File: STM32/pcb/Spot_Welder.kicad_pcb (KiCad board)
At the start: 2 copper layers, 100 x 60 mm, 63 parts, among them J1 SSD1306, J5 Battery, J6 Foot_Switch, SW1 RE, U1 HY4903B6, U10 HY4903B6, U11 HY4903B6, U2 STM32F030F4Px, U3 AMS1117-3.3, U4 ZXGD3009E6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

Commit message: pcb update
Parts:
- added C1: 10u, Capacitor_SMD:C_0805_2012Metric, F.Cu at (115.0, 164.0)
- added D18: TVS_SMDJ13A, Diode_SMD:D_SMC, B.Cu at (124.0, 130.0)
- added D19: TVS_SMDJ13A, Diode_SMD:D_SMC, B.Cu at (100.0, 130.0)
- added D20: TVS_SMDJ13A, Diode_SMD:D_SMC, B.Cu at (112.0, 130.0)
- added D21: TVS_SMDJ13A, Diode_SMD:D_SMC, B.Cu at (88.0, 130.0)
- added H1: MountingHole_Pad, MountingHole:MountingHole_6mm_Pad_Via, F.Cu at (125.0, 110.0)
- added H10: MountingHole_Pad, MountingHole:MountingHole_6mm_Pad_Via, F.Cu at (105.0, 150.0)
- added H11: MountingHole_Pad, MountingHole:MountingHole_6mm_Pad_Via, F.Cu at (145.0, 150.0)
- added H12: MountingHole_Pad, MountingHole:MountingHole_6mm_Pad_Via, F.Cu at (165.0, 150.0)
- added H2: MountingHole_Pad, MountingHole:MountingHole_6mm_Pad_Via, F.Cu at (105.0, 110.0)
- added H3: MountingHole, MountingHole:MountingHole_2.5mm, F.Cu at (177.0, 177.0)
- added H4: MountingHole, MountingHole:MountingHole_2.5mm, F.Cu at (177.0, 93.0)
- added H5: MountingHole, MountingHole:MountingHole_2.5mm, F.Cu at (83.0, 93.0)
- added H6: MountingHole, MountingHole:MountingHole_2.5mm, F.Cu at (83.0, 177.0)
- added H7: MountingHole_Pad, MountingHole:MountingHole_6mm_Pad_Via, F.Cu at (165.0, 110.0)
- added H8: MountingHole_Pad, MountingHole:MountingHole_6mm_Pad_Via, F.Cu at (145.0, 110.0)
- added H9: MountingHole_Pad, MountingHole:MountingHole_6mm_Pad_Via, F.Cu at (125.0, 150.0)
- added R21: 4.7k, Resistor_SMD:R_0603_1608Metric, F.Cu at (146.0, 168.0)
- added R22: 4.7k, Resistor_SMD:R_0603_1608Metric, F.Cu at (146.0, 170.0)
- C6: value 1u -> 10u; footprint Capacitor_SMD:C_0603_1608Metric -> Capacitor_SMD:C_0805_2012Metric
- C7: value 1u -> 22u; footprint Capacitor_SMD:C_0603_1608Metric -> Capacitor_SMD:C_1206_3216Metric
- D10, D11, D12, D13, D14, D15, D16, D17, D5, D7, D8, D9: moved to B.Cu
- R13, R14, R15, R16, R17, R18, R19, R20: value 100 -> 22; moved to B.Cu
- moved U4 117.7 mm to (173.0, 169.0), turned to 90 degrees
- moved U11 115.5 mm to (172.0, 130.0), turned to 90 degrees
- moved SW1 107.7 mm to (158.0, 177.0), turned to 90 degrees
- moved R17 106.4 mm to (160.0, 138.0)
- moved R20 102.7 mm to (172.0, 138.0)
- moved R14 99.2 mm to (148.0, 138.0)
- moved C10 98.4 mm to (174.0, 163.0), turned to 90 degrees
- moved R5 96.9 mm to (178.0, 163.0), turned to -90 degrees
- moved R8 96.6 mm to (170.0, 175.0)
- moved D4 94.0 mm to (171.0, 163.0), turned to 180 degrees
- moved J1 93.0 mm to (138.9, 175.0)
- moved R6 89.3 mm to (176.0, 163.0), turned to 90 degrees
- moved D6 88.7 mm to (177.0, 169.0), turned to -90 degrees
- moved R7 87.6 mm to (170.0, 177.0), turned to 180 degrees
- moved C11 87.3 mm to (170.0, 173.0)
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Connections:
- J1 pad 3: (no net) -> SCL
- J1 pad 4: (no net) -> SDA
- U2 pad 1: (no net) -> Net-(U2-Pad1)
- U2 pad 10: (no net) -> Net-(U2-Pad10)
- U2 pad 11: (no net) -> Net-(U2-Pad11)
- U2 pad 12: (no net) -> Net-(U2-Pad12)
- U2 pad 13: (no net) -> Net-(U2-Pad13)
- U2 pad 14: (no net) -> Net-(U2-Pad14)
- U2 pad 15: (no net) -> Net-(U2-Pad15)
- U2 pad 16: (no net) -> Net-(U2-Pad16)
- U2 pad 17: (no net) -> Net-(U2-Pad17)
- U2 pad 18: (no net) -> Net-(U2-Pad18)
- U2 pad 19: (no net) -> Net-(U2-Pad19)
- U2 pad 2: (no net) -> Net-(U2-Pad2)
- U2 pad 20: (no net) -> Net-(U2-Pad20)
- U2 pad 3: (no net) -> Net-(U2-Pad3)
- U2 pad 4: (no net) -> Net-(U2-Pad4)
- U2 pad 5: (no net) -> Net-(U2-Pad5)
- U2 pad 6: (no net) -> Net-(U2-Pad6)
- U2 pad 7: (no net) -> Net-(U2-Pad7)
- U2 pad 8: (no net) -> Net-(U2-Pad8)
- U2 pad 9: (no net) -> Net-(U2-Pad9)
- U3 pad 1: (no net) -> GND
- U4 pad 2: (no net) -> MCU_Gate
- U4 pad 5: (no net) -> Net-(U4-Pad5)
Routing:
- net Gate_Drive: track 0.00 -> 196.6 mm, vias 0 -> 1
- net 12V_VCC: track 0.00 -> 89.9 mm
- net OUT-: track 0.00 -> 41.9 mm, vias 0 -> 524
- net ADC_Pulse: track 0.00 -> 8.58 mm
- net Net-(R7-Pad2): track 0.00 -> 8.21 mm
- net Net-(R10-Pad1): track 0.00 -> 8.21 mm
- net SCL: track 0.00 -> 8.15 mm
- net Net-(D7-Pad1): track 0.00 -> 7.25 mm, vias 0 -> 1
- net Net-(D9-Pad1): track 0.00 -> 6.99 mm, vias 0 -> 1
- net Net-(D8-Pad1): track 0.00 -> 6.99 mm, vias 0 -> 1
- net Net-(D5-Pad1): track 0.00 -> 6.99 mm, vias 0 -> 1
- net Net-(D13-Pad1): track 0.00 -> 6.99 mm, vias 0 -> 1
- net Net-(D12-Pad1): track 0.00 -> 6.99 mm, vias 0 -> 1
- net Net-(D11-Pad1): track 0.00 -> 6.99 mm, vias 0 -> 1
- net Net-(D10-Pad1): track 0.00 -> 6.99 mm, vias 0 -> 1
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- added copper zone on B.Cu, net GND
- added copper zone on F.Cu, net GND
- added copper zone on B.Cu, net OUT-
- added copper zone on F.Cu, net OUT-
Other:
- board size 100 x 60 mm -> 100 x 90 mm
- net class Default: trace_width 0.25 -> 0.3
- rule trace_min: 0.2 -> 0.3

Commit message: pcb update
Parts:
- moved R13 6.40 mm to (95.0, 134.0), turned to 90 degrees
- moved R14 6.40 mm to (143.0, 134.0), turned to 90 degrees
- moved R15 6.40 mm to (83.0, 134.0), turned to 90 degrees
- moved R16 6.40 mm to (119.0, 134.0), turned to 90 degrees
- moved R17 6.40 mm to (155.0, 134.0), turned to 90 degrees
- moved R18 6.40 mm to (107.0, 134.0), turned to 90 degrees
- moved R19 6.40 mm to (131.0, 134.0), turned to 90 degrees
- moved R20 6.40 mm to (167.0, 134.0), turned to 90 degrees
- moved D10 1.00 mm to (159.0, 136.0)
- moved D11 1.00 mm to (111.0, 136.0)
- moved D12 1.00 mm to (135.0, 136.0)
- moved D13 1.00 mm to (171.0, 136.0)
- moved D5 1.00 mm to (99.0, 136.0)
- moved D7 1.00 mm to (147.0, 136.0)
- moved D8 1.00 mm to (87.0, 136.0)
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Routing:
- net Gate_Drive: track 196.6 -> 152.9 mm
- net 3.3V_MCU: track 2.00 -> 26.0 mm
- net 12V_VCC: track 89.9 -> 109.5 mm
- net +12V: track 0.00 -> 14.2 mm
- net OUT-: track 41.9 -> 36.3 mm
- net ADC_VIN: track 6.74 -> 8.58 mm
- net GND: vias 404 -> 396

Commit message: pcb complete
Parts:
- added C14: 0.1u, Capacitor_SMD:C_0603_1608Metric, F.Cu at (132.2, 164.4)
- added C15: 0.1u, Capacitor_SMD:C_0603_1608Metric, F.Cu at (118.0, 165.8)
- added C2: 1u, Capacitor_SMD:C_0603_1608Metric, F.Cu at (118.0, 162.6)
- added FB1: Ferrite_Bead, Inductor_SMD:L_0603_1608Metric, F.Cu at (118.0, 167.4)
- added J2: Debug, Connector_PinSocket_2.54mm:PinSocket_1x03_P2.54mm_Vertical, F.Cu at (127.5, 177.0)
- added R23: 10k, Resistor_SMD:R_0603_1608Metric, F.Cu at (118.0, 164.2)
- added U12: AT24CS04-STUM, Package_TO_SOT_SMD:SOT-23-5, F.Cu at (140.8, 169.4)
- H1, H10, H11, H12, H2, H7, H8, H9: footprint MountingHole:MountingHole_6mm_Pad_Via -> MountingHole:MountingHole_5mm_Pad
- moved R7 19.5 mm to (151.0, 172.8), turned to 0 degrees
- moved R8 19.4 mm to (151.0, 171.2), turned to 180 degrees
- moved C11 19.3 mm to (151.0, 169.6), turned to 180 degrees
- moved R3 16.1 mm to (131.0, 177.6), turned to 180 degrees
- moved R4 14.0 mm to (131.0, 176.0), turned to 0 degrees
- moved C9 12.1 mm to (131.0, 174.4), turned to 0 degrees
- moved U2 11.2 mm to (125.8, 165.4)
- moved C8 10.2 mm to (118.8, 170.0)
- moved J6 10.0 mm to (116.0, 175.1)
- moved D3 9.93 mm to (131.0, 171.8), turned to 90 degrees
- moved R2 9.85 mm to (117.2, 170.0)
- moved R1 9.45 mm to (115.6, 170.0)
- moved R21 8.12 mm to (138.0, 169.4), turned to -90 degrees
- moved H1 5.00 mm to (120.0, 110.0)
- moved H10 5.00 mm to (100.0, 150.0)
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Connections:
- U2 pad 1: Net-(U2-Pad1) -> GND
- U2 pad 10: Net-(U2-Pad10) -> Foot_Switch
- U2 pad 11: Net-(U2-Pad11) -> ADC_VIN
- U2 pad 12: Net-(U2-Pad12) -> Encoder_A
- U2 pad 13: Net-(U2-Pad13) -> Encoder_B
- U2 pad 14: Net-(U2-Pad14) -> Encoder_Switch
- U2 pad 15: Net-(U2-Pad15) -> GND
- U2 pad 16: Net-(U2-Pad16) -> 3.3V_MCU
- U2 pad 17: Net-(U2-Pad17) -> SCL
- U2 pad 18: Net-(U2-Pad18) -> SDA
- U2 pad 19: Net-(U2-Pad19) -> SWDIO
- U2 pad 20: Net-(U2-Pad20) -> SWCLK
- U2 pad 5: Net-(U2-Pad5) -> /VDDA
- U2 pad 6: Net-(U2-Pad6) -> ADC_Pulse
- U2 pad 7: Net-(U2-Pad7) -> MCU_Gate
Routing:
- net 3.3V_MCU: track 26.0 -> 93.5 mm, vias 0 -> 3
- net MCU_Gate: track 0.00 -> 61.1 mm
- net ADC_Pulse: track 8.58 -> 61.2 mm
- net Encoder_A: track 2.00 -> 28.6 mm
- net SDA: track 5.10 -> 31.2 mm, vias 0 -> 1
- net Encoder_B: track 2.00 -> 24.6 mm
- net Encoder_Switch: track 4.00 -> 25.8 mm
- net SCL: track 8.15 -> 28.9 mm, vias 0 -> 1
- net 12V_VCC: track 109.5 -> 129.4 mm
- net SWCLK: track 0.00 -> 16.8 mm
- net SWDIO: track 0.00 -> 16.1 mm
- net Net-(R7-Pad2): track 8.21 -> 15.4 mm
- net GND: track 0.00 -> 6.00 mm, vias 396 -> 526
- net /VDDA: track 0.00 -> 5.96 mm
- net Net-(C2-Pad1): track 0.00 -> 5.76 mm
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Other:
- board text added: "+"
- board text added: "-"
- board text added: "12V"
- board text added: "Foot SW"
- board text added: "SSD1306"
- board text added: "SWD"

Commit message: pcb update
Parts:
- moved D10 3.00 mm to (159.0, 133.0)
- moved D11 3.00 mm to (111.0, 133.0)
- moved D12 3.00 mm to (135.0, 133.0)
- moved D13 3.00 mm to (171.0, 133.0)
- moved D14 3.00 mm to (160.0, 127.0)
- moved D15 3.00 mm to (148.0, 127.0)
- moved D16 3.00 mm to (136.0, 127.0)
- moved D17 3.00 mm to (172.0, 127.0)
- moved D18 3.00 mm to (124.0, 127.0)
- moved D19 3.00 mm to (100.0, 127.0)
- moved D20 3.00 mm to (112.0, 127.0)
- moved D21 3.00 mm to (88.0, 127.0)
- moved D5 3.00 mm to (99.0, 133.0)
- moved D7 3.00 mm to (147.0, 133.0)
- moved D8 3.00 mm to (87.0, 133.0)
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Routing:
- net OUT-: track 36.3 -> 39.3 mm, vias 616 -> 110
- net Gate_Drive: track 154.5 -> 157.5 mm
- net GND: track 6.00 -> 5.50 mm, vias 526 -> 133

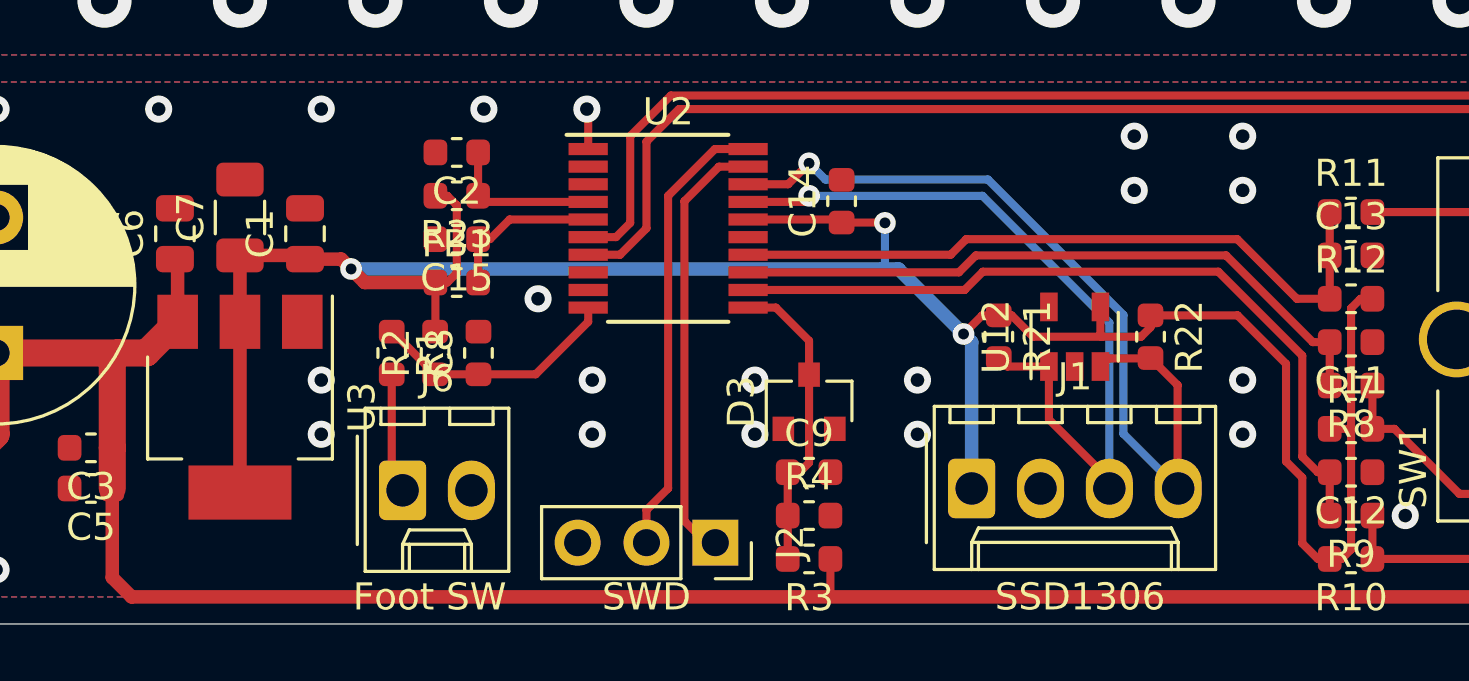
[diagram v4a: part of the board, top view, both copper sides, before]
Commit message: eeprom footprint changed
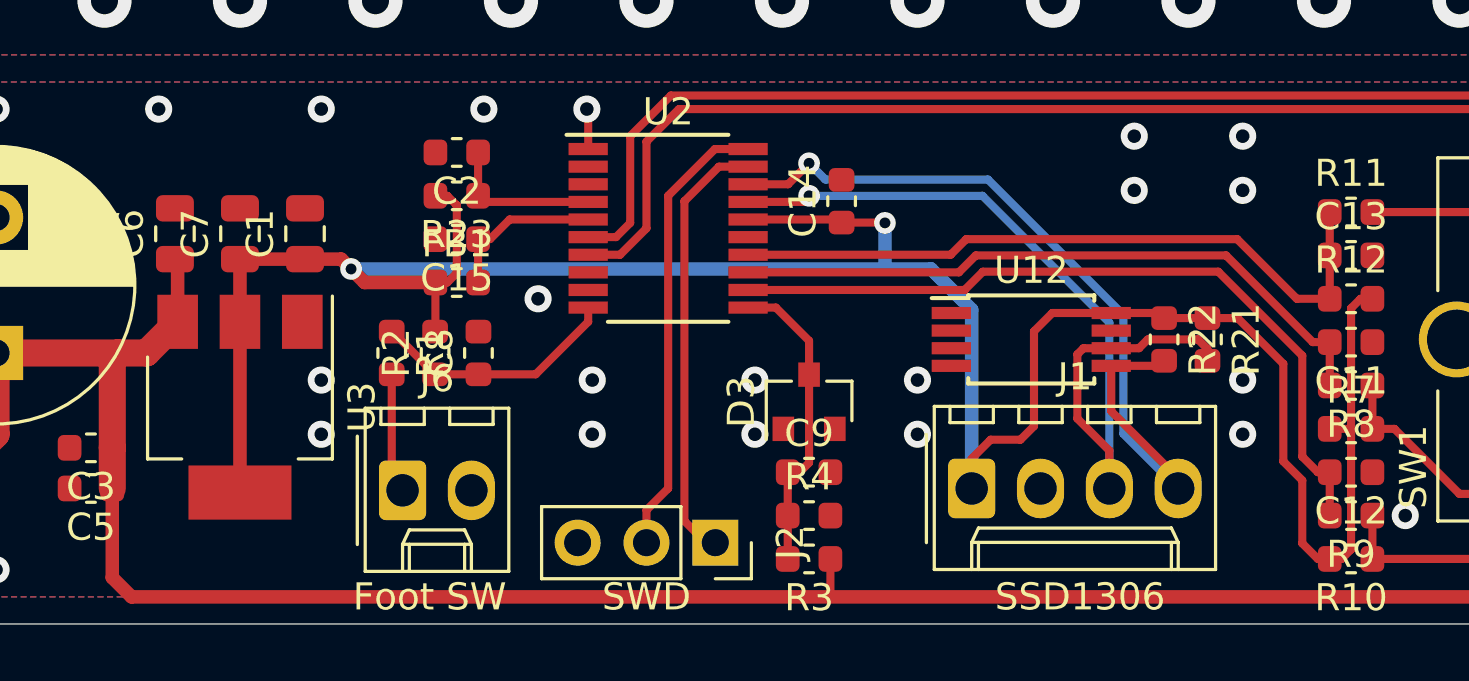
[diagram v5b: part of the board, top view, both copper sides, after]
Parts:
- C7: footprint Capacitor_SMD:C_1206_3216Metric -> Capacitor_SMD:C_0805_2012Metric
- U12: value AT24CS04-STUM -> 24LC64; footprint Package_TO_SOT_SMD:SOT-23-5 -> Package_SO:TSSOP-8_4.4x3mm_P0.65mm
- moved R21 7.70 mm to (145.7, 169.5)
- moved U12 1.60 mm to (139.2, 169.5), turned to 0 degrees
- moved C7 0.60 mm to (110.0, 165.6)
- moved R22 0.51 mm to (144.1, 169.5)
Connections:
- U12 pad 1: SCL -> GND
- U12 pad 3: SDA -> GND
- U12 pad 4: 3.3V_MCU -> GND
- U12 pad 5: GND -> SDA
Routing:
- net SCL: track 28.9 -> 32.9 mm
- net 3.3V_MCU: track 93.5 -> 96.9 mm, vias 3 -> 2
